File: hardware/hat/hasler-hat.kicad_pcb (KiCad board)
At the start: 4 copper layers, 85 x 41 mm, 116 parts, among them J1 Amp4 top header, J2 Hasler J2, J3 USB-C PD in, J4 Debug / expansion, J5 Qwiic, J6 To Amp4 DC in, U1 MCP23017, U10 SRV05-4, U11 SRV05-4, U12 SRV05-4, U2 ADS1115, U3 CH224A, U4 TPS259474ARPWR, U6 XC6206P332MR, U7 SRV05-4, U8 SRV05-4, U9 SRV05-4

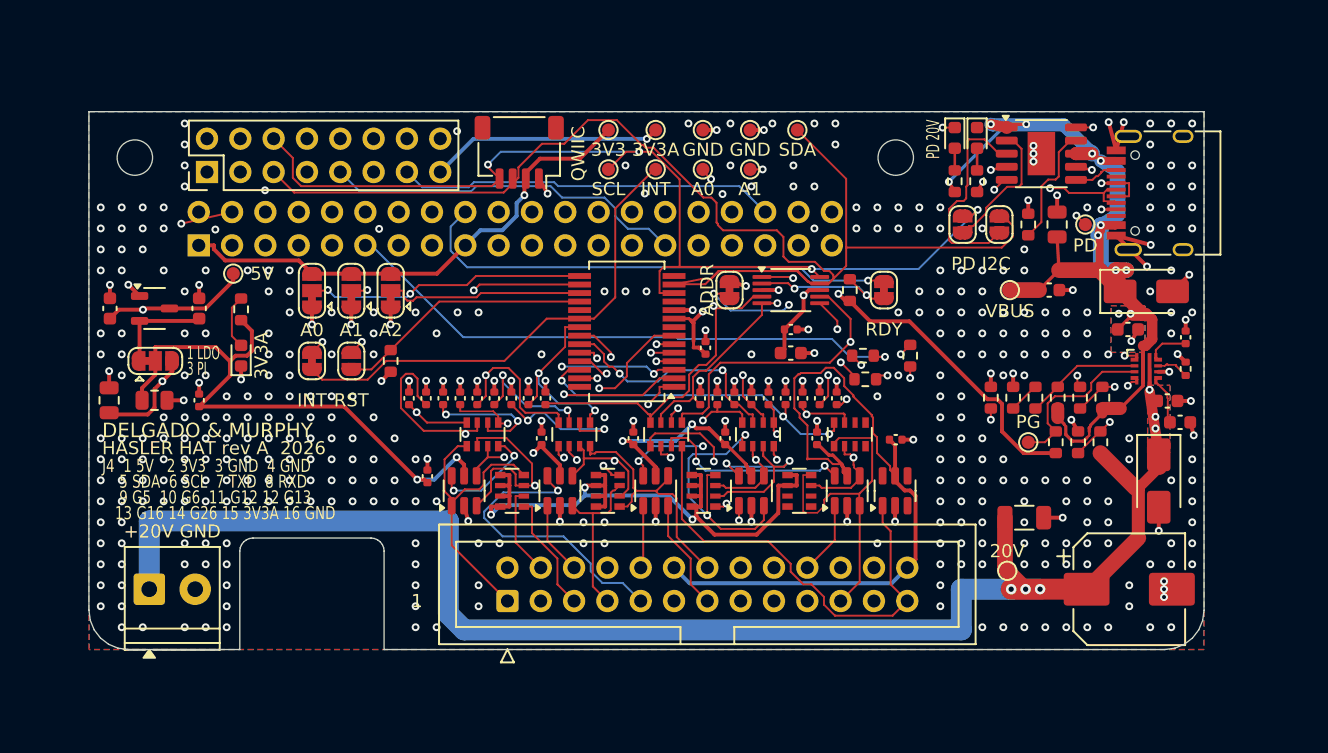
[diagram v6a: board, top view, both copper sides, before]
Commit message: HAT: eFuse turns on at the charger's 5 V (JP11 for 10.3 V), CH224A cap under the chip, review round 4
A start-up model with the Amp4's measured 220 uF and the Pi booting part-way up the
ramp showed the eFuse could overheat and restart for ever with a 10.3 V UVLO, at any
ramp rate. With JP11 open (as shipped) EN is pulled up by R3 alone, so U4 is fully
on before the PD contract and the 5 -> 20 V step costs it nothing; bridging JP11
restores the 10.3 V UVLO. C1 moved right under the CH224A (was ~20 mm of copper away).
In2 links for 3V3A (C41-C42), ADS_RDY and SDA. Bottom silk: eFuse line fixed,
JLC placeholder removed, an easter egg. Zip without the job file and drill maps.
check.py (fast netlist/BOM/threshold check, run by build.sh). Docs: start-up
analysis, 3V3A current limit, bring-up, edge rails, round-4 review. Renders without C7.

Co-Authored-By: Claude Opus 5.5 <noreply@anthropic.com>
Claude-Session: https://claude.ai/code/session_014wovV18Ypx4LXt9k8BSCRk
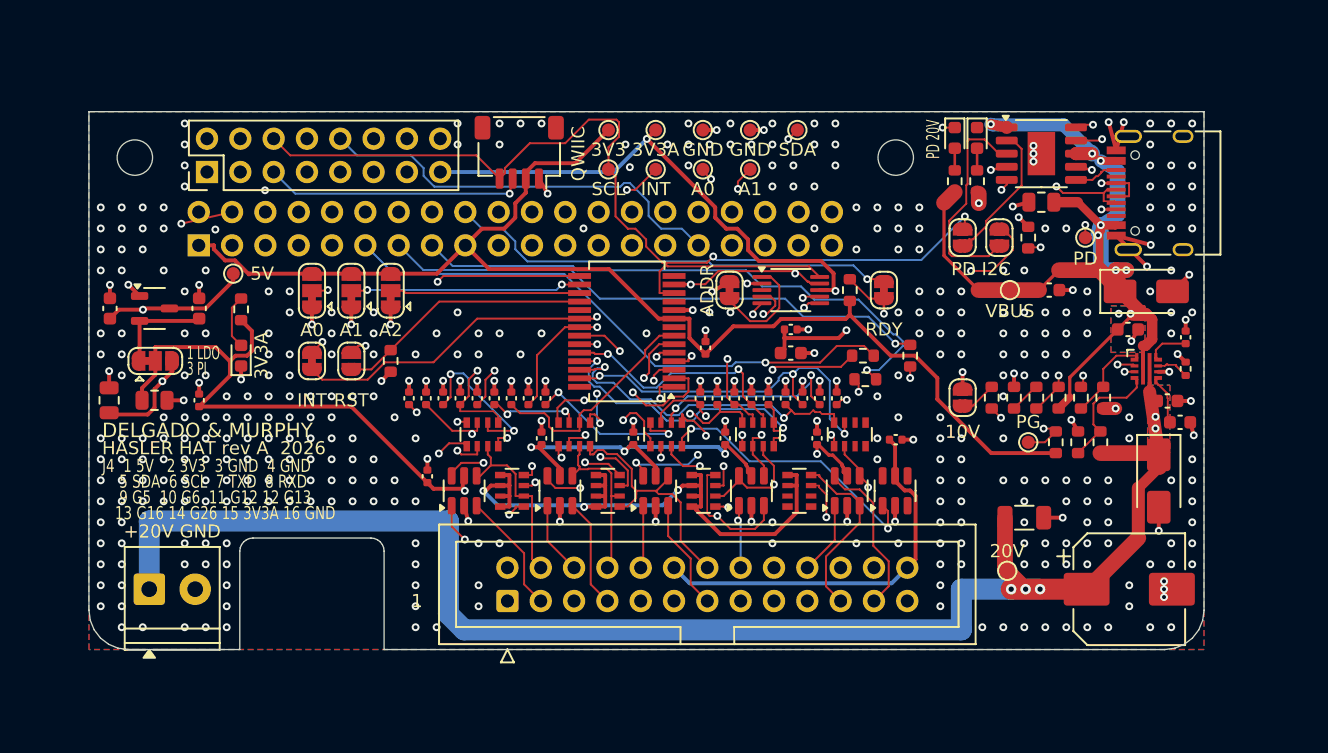
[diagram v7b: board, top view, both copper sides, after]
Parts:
- added JP11: UVLO_10V, Jumper:SolderJumper-2_P1.3mm_Open_RoundedPad1.0x1.5mm, F.Cu at (166.6, 121.8)
- moved C1 2.08 mm to (172.6, 106.9), turned to 180 degrees
- moved JP10 1.00 mm to (169.4, 109.6)
- moved JP9 1.00 mm to (166.6, 109.6)
- moved R1 1.00 mm to (171.6, 109.6)
- moved TP11 1.00 mm to (175.9, 109.6)
- moved R16 0.07 mm to (168.8, 121.8)
- moved R3 0.07 mm to (177.3, 121.8)
- moved R5 0.07 mm to (173.9, 121.8)
- moved R7 0.07 mm to (170.5, 121.8)
- moved R4 0.07 mm to (175.6, 121.8)
- moved R6 0.07 mm to (172.2, 121.8)
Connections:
- R16 pad 2: /GND -> /EF_ENJ
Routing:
- net /SDA: track 118.6 -> 94.8 mm, vias 0 -> 5
- net /3V3A: track 225.0 -> 201.7 mm, vias 7 -> 8
- net /J_A0: track 44.4 -> 24.3 mm
- net /MCP_INTA: track 37.1 -> 52.0 mm, vias 0 -> 2
- net /J_A2: track 27.1 -> 39.1 mm, vias 2 -> 1
- net /M_PU: track 28.6 -> 17.6 mm, vias 3 -> 0
- net /VBUS: track 82.3 -> 92.5 mm, vias 11 -> 10
- net /J_K2: track 24.8 -> 35.0 mm, vias 1 -> 2
- net /J_LG: track 44.7 -> 34.6 mm
- net /J_X3: track 27.9 -> 18.8 mm, vias 2 -> 1
- net /VOUT: track 144.1 -> 151.8 mm, vias 7 -> 6
- net /J_A3: track 35.0 -> 27.8 mm, vias 0 -> 2
- net /M_K5: track 29.9 -> 22.8 mm, vias 2 -> 3
- net /PD_CFG1: track 9.32 -> 16.4 mm, vias 0 -> 2
- net /M_K4: track 21.9 -> 28.5 mm
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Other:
- board text added: "(U4 won't let you)"
- board text added: "10V"
- board text added: "Bigger on the inside."
- board text added: "JP11 shut: UV 10.3V"
- board text added: "OF THE NEUTRON FLOW"
- board text added: "REVERSE THE POLARITY"
- board text added: "eFuse OV 22.6V 3.3A"
- board text removed: "JLCJLCJLCJLC"
- board text removed: "eFuse 11.2-23 V 3.3 A"

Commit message: HAT: C1 linked to U3's VBUS on B.Cu; review pass 2 fixes
Board: a short bottom-layer link from C1 to the CH224A's pin-8 VBUS via (C1 was fed
from J3's side, ~15 mm). DRC clean, fab files regenerated.
Daemon: the MCP23017's IPOL is checked on every read and a sample taken after a
reset is dropped (a reset can no longer show as every key pressed or arm the end
switch); the end switch arms only after reading on for a debounce time.
Docs: the start-up trade-offs (PD standby/capacitance, charger slew, retry at 20 V ->
re-plug, brown-out wording), 20V LED, PG bench check, JP11 location, scope check,
C7 paste, renders note, build-guide HAT note, stale comments.

Co-Authored-By: Claude Opus 5.5 <noreply@anthropic.com>
Claude-Session: https://claude.ai/code/session_014wovV18Ypx4LXt9k8BSCRk
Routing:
- net /VBUS: track 92.5 -> 99.6 mm, vias 10 -> 11
